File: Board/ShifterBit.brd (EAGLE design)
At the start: 27.2 x 60.5 mm, 13 parts

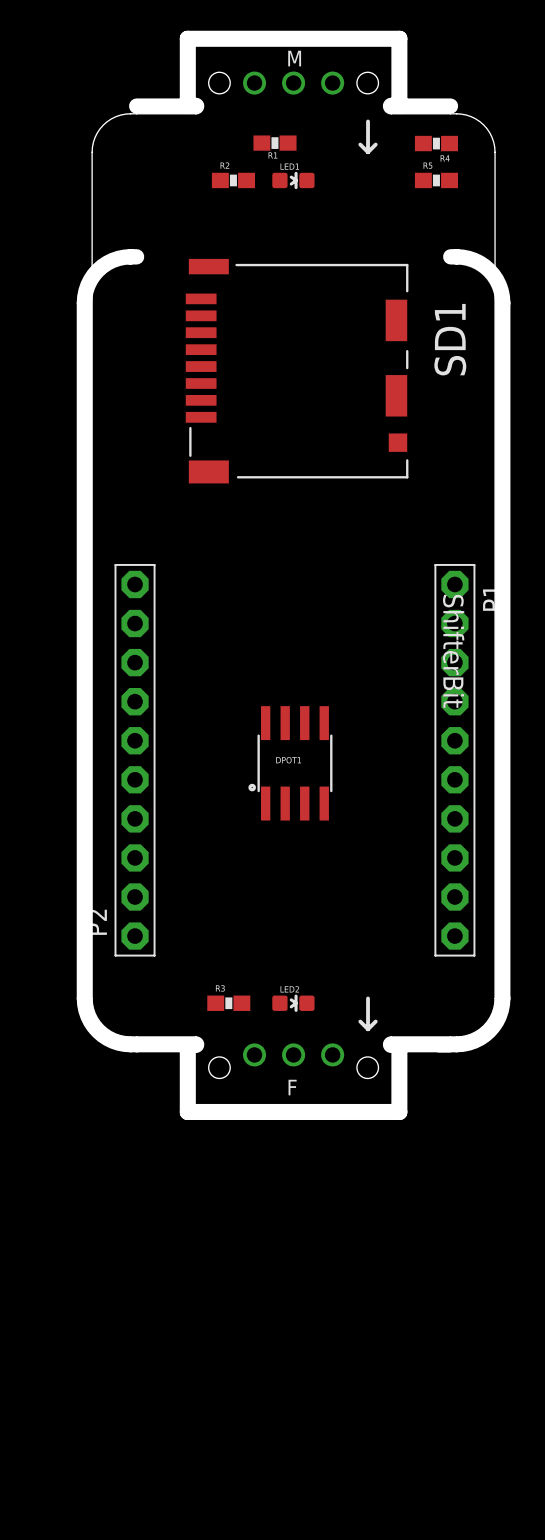
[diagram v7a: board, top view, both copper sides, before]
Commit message: better placement
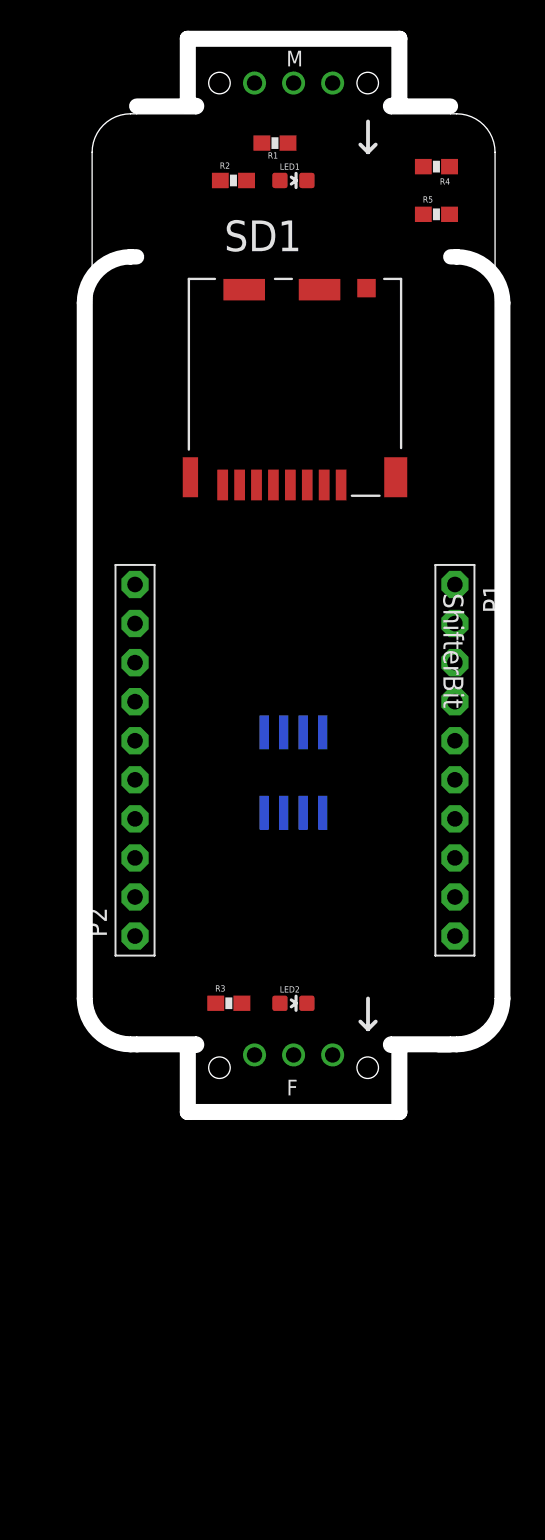
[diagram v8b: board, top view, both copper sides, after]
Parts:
- moved SD1 10.1 mm to (16.3, 40.5), turned to 0 degrees
- moved R5 2.20 mm to (22.5, 58.1)
- moved R4 1.50 mm to (22.5, 61.2)
- moved DPOT1 0.61 mm to (13.2, 21.8), flipped to the bottom, turned to 180 degrees
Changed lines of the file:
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@@
 <autorouter>
 <pass name="Default">
-<param name="RoutingGrid" value="50mil"/>
+<param name="RoutingGrid" value="0.125mm"/>
 <param name="AutoGrid" value="1"/>
 <param name="Efforts" value="2"/>
@@
 <element name="P1" library="adafruit" package="1X10-BIG" value="" x="23.7" y="22.6" rot="R270"/>
 <element name="P2" library="adafruit" package="1X10-BIG" value="" x="2.9" y="22.6" rot="R90"/>
-<element name="SD1" library="HIROSE-DM3CS-SF" package="HIROSE_DM3CS-SF" value="" x="7.2" y="44.9" rot="R270">
-<attribute name="OC_NEWARK" value="35R0581" x="7.2" y="44.9" size="1.778" layer="27" rot="R270" display="off"/>
-<attribute name="MPN" value="DM3CS-SF" x="7.2" y="44.9" size="1.778" layer="27" rot="R270" display="off"/>
-<attribute name="SUPPLIER" value="HIROSE" x="7.2" y="44.9" size="1.778" layer="27" rot="R270" display="off"/>
-<attribute name="OC_FARNELL" value="1764376" x="7.2" y="44.9" size="1.778" layer="27" rot="R270" display="off"/>
-<attribute name="PACKAGE" value="SMD - microSD" x="7.2" y="44.9" size="1.778" layer="27" rot="R270" display="off"/>
+<element name="SD1" library="HIROSE-DM3CS-SF" package="HIROSE_DM3CS-SF" value="" x="16.3" y="40.5">
+<attribute name="OC_NEWARK" value="35R0581" x="16.3" y="40.5" size="1.778" layer="27" display="off"/>
+<attribute name="MPN" value="DM3CS-SF" x="16.3" y="40.5" size="1.778" layer="27" display="off"/>
+<attribute name="SUPPLIER" value="HIROSE" x="16.3" y="40.5" size="1.778" layer="27" display="off"/>
+<attribute name="OC_FARNELL" value="1764376" x="16.3" y="40.5" size="1.778" layer="27" display="off"/>
+<attribute name="PACKAGE" value="SMD - microSD" x="16.3" y="40.5" size="1.778" layer="27" display="off"/>
 </element>
 <element name="LED1" library="SparkFun-LED" package="LED-0603" value="" x="13.2" y="60.3" rot="R270">
@@
 <element name="R2" library="SparkFun-Passives" package="0603-RES" value="56" x="9.3" y="60.3"/>
 <element name="R3" library="SparkFun-Passives" package="0603-RES" value="56" x="9" y="6.8"/>
-<element name="R4" library="SparkFun-Passives" package="0603-RES" value="2K2" x="22.5" y="62.7" rot="R180"/>
-<element name="R5" library="SparkFun-Passives" package="0603-RES" value="560" x="22.5" y="60.3"/>
-<element name="DPOT1" library="SparkFun-AnalogIC" package="SO08" value="MCP41XXX" x="13.3" y="22.4"/>
+<element name="R4" library="SparkFun-Passives" package="0603-RES" value="2K2" x="22.5" y="61.2" rot="R180"/>
+<element name="R5" library="SparkFun-Passives" package="0603-RES" value="560" x="22.5" y="58.1"/>
+<element name="DPOT1" library="SparkFun-AnalogIC" package="SO08" value="MCP41XXX" x="13.2" y="21.8" rot="MR180"/>
 </elements>
 <signals>
@@
 <wire x1="11.15" y1="62.73" x2="10.67" y2="66.635" width="0" layer="19" extent="1-1"/>
 <wire x1="14.077" y1="60.3" x2="11.15" y2="62.73" width="0" layer="19" extent="1-1"/>
-<wire x1="21.65" y1="60.3" x2="14.077" y2="60.3" width="0" layer="19" extent="1-1"/>
-<wire x1="19.9" y1="51.2" x2="21.65" y2="60.3" width="0" layer="19" extent="1-1"/>
-<wire x1="12.665" y1="25.0162" x2="19.9" y2="51.2" width="0" layer="19" extent="1-1"/>
-<wire x1="7.2" y1="50.4" x2="12.665" y2="25.0162" width="0" layer="19" extent="1-1"/>
-<wire x1="7.7" y1="54.7" x2="7.2" y2="50.4" width="0" layer="19" extent="1-1"/>
-<wire x1="15.205" y1="19.7838" x2="12.665" y2="25.0162" width="0" layer="19" extent="1-1"/>
-<wire x1="20" y1="43.25" x2="15.205" y2="19.7838" width="0" layer="19" extent="1-1"/>
-<wire x1="7.7" y1="41.35" x2="15.205" y2="19.7838" width="0" layer="19" extent="1-1"/>
-<wire x1="2.9" y1="11.17" x2="7.7" y2="41.35" width="0" layer="19" extent="1-1"/>
-<wire x1="23.7" y1="11.17" x2="20" y2="43.25" width="0" layer="19" extent="1-1"/>
-<wire x1="14.077" y1="6.8" x2="23.7" y2="11.17" width="0" layer="19" extent="1-1"/>
-<wire x1="10.67" y1="3.44" x2="14.077" y2="6.8" width="0" layer="19" extent="1-1"/>
+<wire x1="21.65" y1="58.1" x2="14.077" y2="60.3" width="0" layer="19" extent="1-1"/>
+<wire x1="17.95" y1="53.3" x2="21.65" y2="58.1" width="0" layer="19" extent="1-1"/>
+<wire x1="10" y1="53.2" x2="17.95" y2="53.3" width="0" layer="19" extent="1-1"/>
+<wire x1="19.85" y1="41" x2="17.95" y2="53.3" width="0" layer="19" extent="1-1"/>
+<wire x1="10.8" y1="40.5" x2="19.85" y2="41" width="0" layer="19" extent="1-1"/>
+<wire x1="6.5" y1="41" x2="10.8" y2="40.5" width="0" layer="19" extent="1-1"/>
+<wire x1="15.105" y1="24.4162" x2="10.8" y2="40.5" width="0" layer="19" extent="1-16"/>
+<wire x1="12.565" y1="19.1838" x2="15.105" y2="24.4162" width="0" layer="19" extent="16-16"/>
+<wire x1="2.9" y1="11.17" x2="12.565" y2="19.1838" width="0" layer="19" extent="16-16"/>
+<wire x1="10.67" y1="3.44" x2="2.9" y2="11.17" width="0" layer="19" extent="1-1"/>
+<wire x1="14.077" y1="6.8" x2="10.67" y2="3.44" width="0" layer="19" extent="1-1"/>
+<wire x1="23.7" y1="11.17" x2="14.077" y2="6.8" width="0" layer="19" extent="1-1"/>
 </signal>
 <signal name="VCC">
@@
 <contactref element="BSF1" pad="VCC"/>
 <contactref element="DPOT1" pad="5"/>
-<wire x1="15.205" y1="25.0162" x2="15.75" y2="66.635" width="0" layer="19" extent="1-1"/>
-<wire x1="15.75" y1="3.44" x2="15.205" y2="25.0162" width="0" layer="19" extent="1-1"/>
+<wire x1="15.105" y1="19.1838" x2="15.75" y2="66.635" width="0" layer="19" extent="16-16"/>
+<wire x1="15.75" y1="3.44" x2="15.105" y2="19.1838" width="0" layer="19" extent="16-16"/>
 </signal>
 <signal name="SIG_OUT">
 <contactref element="BSF1" pad="SIG"/>
 <contactref element="DPOT1" pad="6"/>
-<wire x1="13.21" y1="3.44" x2="13.935" y2="25.0162" width="0" layer="19" extent="1-1"/>
+<wire x1="13.21" y1="3.44" x2="13.835" y2="19.1838" width="0" layer="19" extent="16-16"/>
 </signal>
 <signal name="SIG_IN">
@@
 <contactref element="R1" pad="2"/>
 <contactref element="R4" pad="2"/>
-<wire x1="12.85" y1="62.73" x2="13.21" y2="66.635" width="0" layer="19" extent="16-16"/>
-<wire x1="21.65" y1="62.7" x2="12.85" y2="62.73" width="0" layer="19" extent="1-16"/>
+<wire x1="12.85" y1="62.73" x2="21.65" y2="61.2" width="0" layer="19" extent="1-1"/>
+<wire x1="13.21" y1="66.635" x2="12.85" y2="62.73" width="0" layer="19" extent="1-1"/>
 </signal>
 <signal name="RST">
@@
 <contactref element="R5" pad="2"/>
 <contactref element="R4" pad="1"/>
-<wire x1="23.35" y1="62.7" x2="23.7" y2="31.49" width="0" layer="19" extent="1-1"/>
-<wire x1="23.35" y1="60.3" x2="23.35" y2="62.7" width="0" layer="19" extent="1-1"/>
+<wire x1="23.35" y1="58.1" x2="23.35" y2="61.2" width="0" layer="19" extent="1-1"/>
+<wire x1="23.7" y1="31.49" x2="23.35" y2="58.1" width="0" layer="19" extent="1-1"/>
 </signal>
 <signal name="EN">
@@
 <contactref element="P1" pad="4"/>
 <contactref element="DPOT1" pad="1"/>
-<wire x1="11.395" y1="19.7838" x2="23.7" y2="26.41" width="0" layer="19" extent="1-1"/>
+<wire x1="11.295" y1="24.4162" x2="23.7" y2="26.41" width="0" layer="19" extent="16-16"/>
 </signal>
 <signal name="D14">
@@
 <contactref element="SD1" pad="5"/>
 <contactref element="DPOT1" pad="2"/>
-<wire x1="7.2" y1="49.3" x2="23.7" y2="23.87" width="0" layer="19" extent="16-16"/>
-<wire x1="12.665" y1="19.7838" x2="7.2" y2="49.3" width="0" layer="19" extent="16-16"/>
+<wire x1="12.565" y1="24.4162" x2="11.9" y2="40.5" width="0" layer="19" extent="1-16"/>
+<wire x1="23.7" y1="23.87" x2="12.565" y2="24.4162" width="0" layer="19" extent="16-16"/>
 </signal>
 <signal name="D12">
 <contactref element="P1" pad="6"/>
 <contactref element="SD1" pad="7"/>
-<wire x1="7.2" y1="51.5" x2="23.7" y2="21.33" width="0" layer="19" extent="16-16"/>
+<wire x1="23.7" y1="21.33" x2="9.7" y2="40.5" width="0" layer="19" extent="1-1"/>
 </signal>
 <signal name="D13">
@@
 <contactref element="SD1" pad="3"/>
 <contactref element="DPOT1" pad="3"/>
-<wire x1="7.2" y1="47.1" x2="23.7" y2="18.79" width="0" layer="19" extent="16-16"/>
-<wire x1="13.935" y1="19.7838" x2="23.7" y2="18.79" width="0" layer="19" extent="1-1"/>
+<wire x1="13.835" y1="24.4162" x2="14.1" y2="40.5" width="0" layer="19" extent="1-16"/>
+<wire x1="23.7" y1="18.79" x2="13.835" y2="24.4162" width="0" layer="19" extent="16-16"/>
 </signal>
 <signal name="V+">
@@
 <contactref element="P2" pad="4"/>
 <contactref element="SD1" pad="2"/>
-<wire x1="2.9" y1="18.79" x2="7.2" y2="46" width="0" layer="19" extent="16-16"/>
+<wire x1="2.9" y1="18.79" x2="15.2" y2="40.5" width="0" layer="19" extent="1-1"/>
 </signal>
 <signal name="3V">
@@
 <contactref element="SD1" pad="4"/>
 <contactref element="DPOT1" pad="8"/>
-<wire x1="2.9" y1="16.25" x2="7.2" y2="48.2" width="0" layer="19" extent="16-16"/>
-<wire x1="11.395" y1="25.0162" x2="2.9" y2="16.25" width="0" layer="19" extent="1-1"/>
+<wire x1="11.295" y1="19.1838" x2="13" y2="40.5" width="0" layer="19" extent="1-16"/>
+<wire x1="2.9" y1="16.25" x2="11.295" y2="19.1838" width="0" layer="19" extent="16-16"/>
 </signal>
 <signal name="LD0">
@@
 <contactref element="R3" pad="2"/>
 <contactref element="LED2" pad="A"/>
-<wire x1="12.323" y1="6.8" x2="9.85" y2="6.8" width="0" layer="19" extent="1-1"/>
+<wire x1="9.85" y1="6.8" x2="12.323" y2="6.8" width="0" layer="19" extent="1-1"/>
 </signal>
 </signals>
